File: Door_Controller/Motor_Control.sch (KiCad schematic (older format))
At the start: 15 parts

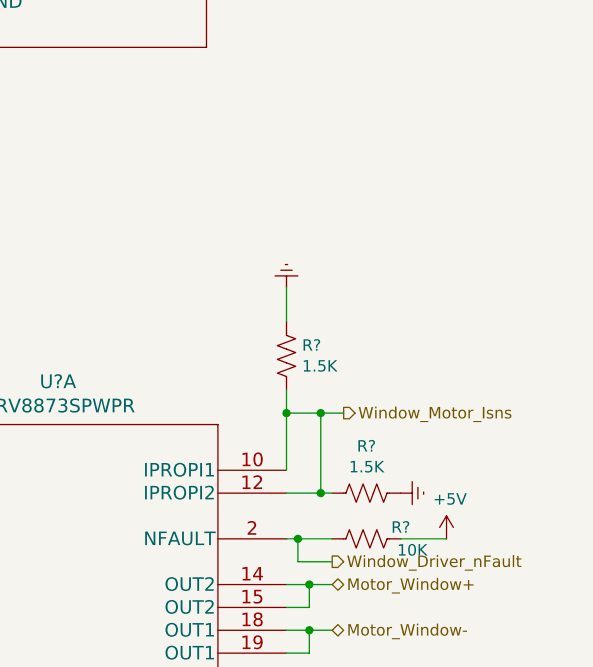
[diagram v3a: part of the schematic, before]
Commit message: differential window motor current sense output in motor control sheet
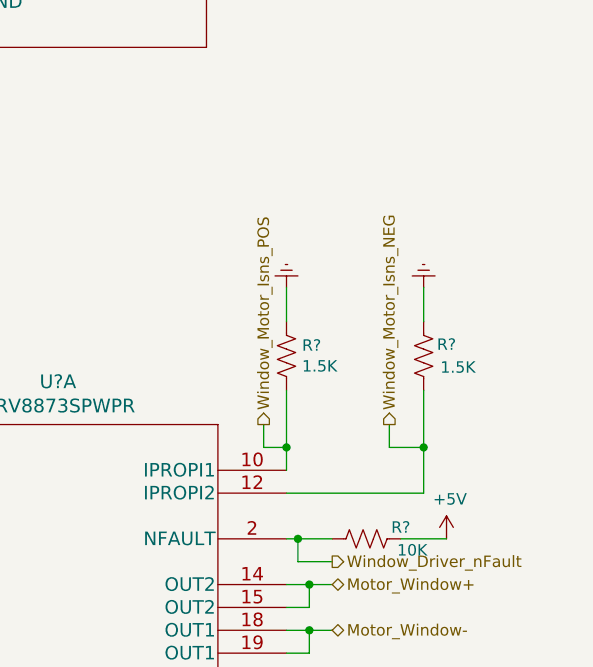
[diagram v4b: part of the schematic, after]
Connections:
- net Window_Motor_Isns renamed Window_Motor_Isns_NEG
- net Window_Motor_Isns_NEG: no longer R?.2, U?.10 (IPROPI1)
- new net Window_Motor_Isns_POS: R?.2, U?.10 (IPROPI1)
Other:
- moved on the sheet: R?
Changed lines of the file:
@@
 L power:Earth #PWR?
 U 1 1 5FB97E86
-P 5300 4650
-F 0 "#PWR?" H 5300 4400 50  0001 C CNN
-F 1 "Earth" H 5300 4500 50  0001 C CNN
-F 2 "" H 5300 4650 50  0001 C CNN
-F 3 "~" H 5300 4650 50  0001 C CNN
-	1    5300 4650
-	0    -1   -1   0
+P 5400 3750
+F 0 "#PWR?" H 5400 3500 50  0001 C CNN
+F 1 "Earth" H 5400 3600 50  0001 C CNN
+F 2 "" H 5400 3750 50  0001 C CNN
+F 3 "~" H 5400 3750 50  0001 C CNN
+	1    5400 3750
+	-1   0    0    1
 $EndComp
 $Comp
@@
 Wire Notes Line
 	3050 5900 3050 5500
-Text HLabel 5050 4300 2    50   Output ~ 0
-Window_Motor_Isns
 Wire Wire Line
 	2650 5550 2800 5550
@@
 Wire Wire Line
 	5000 5550 4800 5550
-$Comp
-L Device:R_US R?
-U 1 1 5FB94200
-P 4800 4050
-F 0 "R?" H 4868 4096 50  0000 L CNN
-F 1 "1.5K" H 4868 4005 50  0000 L CNN
-F 2 "" V 4840 4040 50  0001 C CNN
-F 3 "~" H 4800 4050 50  0001 C CNN
-	1    4800 4050
-	1    0    0    -1
-$EndComp
-$Comp
-L power:Earth #PWR?
-U 1 1 5FB972EF
-P 4800 3750
-F 0 "#PWR?" H 4800 3500 50  0001 C CNN
-F 1 "Earth" H 4800 3600 50  0001 C CNN
-F 2 "" H 4800 3750 50  0001 C CNN
-F 3 "~" H 4800 3750 50  0001 C CNN
-	1    4800 3750
-	-1   0    0    1
-$EndComp
-Wire Wire Line
-	4800 4650 4950 4650
-Wire Wire Line
-	4800 3900 4800 3750
-Connection ~ 4800 4300
-Wire Wire Line
-	4800 4300 4800 4200
-Wire Wire Line
-	4950 4650 4950 4300
-Connection ~ 4950 4650
-Wire Wire Line
-	4950 4650 5000 4650
-Connection ~ 4950 4300
-Wire Wire Line
-	4950 4300 4800 4300
-Wire Wire Line
-	5050 4300 4950 4300
 Text HLabel 5000 4950 2    50   Output ~ 0
 Window_Driver_nFault
@@
 Wire Wire Line
 	4850 4850 5000 4850
-Wire Wire Line
-	4800 4550 4800 4300
+$Comp
+L Device:R_US R?
+U 1 1 5FB96318
+P 5400 4050
+F 0 "R?" H 5500 4100 50  0000 C CNN
+F 1 "1.5K" H 5550 4000 50  0000 C CNN
+F 2 "" V 5440 4040 50  0001 C CNN
+F 3 "~" H 5400 4050 50  0001 C CNN
+	1    5400 4050
+	1    0    0    -1
+$EndComp
+$Comp
+L power:Earth #PWR?
+U 1 1 5FBE9744
+P 2300 4650
+F 0 "#PWR?" H 2300 4400 50  0001 C CNN
+F 1 "Earth" H 2300 4500 50  0001 C CNN
+F 2 "" H 2300 4650 50  0001 C CNN
+F 3 "~" H 2300 4650 50  0001 C CNN
+	1    2300 4650
+	0    1    1    0
+$EndComp
+$Comp
+L power:Earth #PWR?
+U 1 1 5FBEA1C6
+P 2300 4950
+F 0 "#PWR?" H 2300 4700 50  0001 C CNN
+F 1 "Earth" H 2300 4800 50  0001 C CNN
+F 2 "" H 2300 4950 50  0001 C CNN
+F 3 "~" H 2300 4950 50  0001 C CNN
+	1    2300 4950
+	0    1    1    0
+$EndComp
+$Comp
+L Device:R_US R?
+U 1 1 5FBEA830
+P 2550 4950
+F 0 "R?" V 2600 5100 50  0000 C CNN
+F 1 "1.5K" V 2500 5100 50  0000 C CNN
+F 2 "" V 2590 4940 50  0001 C CNN
+F 3 "~" H 2550 4950 50  0001 C CNN
+	1    2550 4950
+	0    1    1    0
+$EndComp
+Wire Wire Line
+	2700 4950 2800 4950
+Wire Wire Line
+	2400 4950 2300 4950
+$Comp
+L Device:R_US R?
+U 1 1 5FBED892
+P 2550 4650
+F 0 "R?" V 2600 4800 50  0000 C CNN
+F 1 "1.5K" V 2500 4800 50  0000 C CNN
+F 2 "" V 2590 4640 50  0001 C CNN
+F 3 "~" H 2550 4650 50  0001 C CNN
+	1    2550 4650
+	0    1    1    0
+$EndComp
+Wire Wire Line
+	2300 4650 2400 4650
+Wire Wire Line
+	2700 4650 2800 4650
+$Comp
+L power:Earth #PWR?
+U 1 1 5FBF1639
+P 1400 5400
+F 0 "#PWR?" H 1400 5150 50  0001 C CNN
+F 1 "Earth" H 1400 5250 50  0001 C CNN
+F 2 "" H 1400 5400 50  0001 C CNN
+F 3 "~" H 1400 5400 50  0001 C CNN
+	1    1400 5400
+	1    0    0    -1
+$EndComp
+$Comp
+L Device:C C?
+U 1 1 5FBF1C79
+P 1400 5150
+F 0 "C?" H 1515 5196 50  0000 L CNN
+F 1 "1uF" H 1515 5105 50  0000 L CNN
+F 2 "" H 1438 5000 50  0001 C CNN
+F 3 "~" H 1400 5150 50  0001 C CNN
+	1    1400 5150
+	1    0    0    -1
+$EndComp
+$Comp
+L power:+5V #PWR?
+U 1 1 5FBF2E2E
+P 1400 4800
+F 0 "#PWR?" H 1400 4650 50  0001 C CNN
+F 1 "+5V" H 1415 4973 50  0000 C CNN
+F 2 "" H 1400 4800 50  0001 C CNN
+F 3 "" H 1400 4800 50  0001 C CNN
+	1    1400 4800
+	1    0    0    -1
+$EndComp
+Wire Wire Line
+	1400 5400 1400 5300
+Wire Wire Line
+	1400 5000 1400 4850
+Wire Wire Line
+	2800 4850 1400 4850
+Connection ~ 1400 4850
+Wire Wire Line
+	1400 4850 1400 4800
+Text HLabel 2350 4550 0    50   Input ~ 0
+Window_Ctrl_nDisable
+$Comp
+L Device:C C?
+U 1 1 5FBF9A3D
+P 2500 4300
+F 0 "C?" H 2615 4346 50  0000 L CNN
+F 1 "1uF" H 2615 4255 50  0000 L CNN
+F 2 "" H 2538 4150 50  0001 C CNN
+F 3 "~" H 2500 4300 50  0001 C CNN
+	1    2500 4300
+	1    0    0    -1
+$EndComp
+$Comp
+L power:Earth #PWR?
+U 1 1 5FBFA2FE
+P 2500 4050
+F 0 "#PWR?" H 2500 3800 50  0001 C CNN
+F 1 "Earth" H 2500 3900 50  0001 C CNN
+F 2 "" H 2500 4050 50  0001 C CNN
+F 3 "~" H 2500 4050 50  0001 C CNN
+	1    2500 4050
+	-1   0    0    1
+$EndComp
+Wire Wire Line
+	2500 4050 2500 4150
+Wire Wire Line
+	2350 4550 2500 4550
+Wire Wire Line
+	2500 4450 2500 4550
+Connection ~ 2500 4550
+Wire Wire Line
+	2500 4550 2800 4550
+Wire Wire Line
+	4800 4650 5400 4650
+Wire Wire Line
+	5400 4650 5400 4450
+Wire Wire Line
+	5400 3900 5400 3750
+Text HLabel 4700 4350 1    50   Output ~ 0
+Window_Motor_Isns_POS
+Text HLabel 5250 4350 1    50   Output ~ 0
+Window_Motor_Isns_NEG
+Wire Wire Line
+	4800 4200 4800 4450
 $Comp
 L DRV8873SPWPR:DRV8873SPWPR U?
@@
 	1    0    0    -1
 $EndComp
-$Comp
-L Device:R_US R?
-U 1 1 5FB96318
-P 5150 4650
-F 0 "R?" V 4945 4650 50  0000 C CNN
-F 1 "1.5K" V 5036 4650 50  0000 C CNN
-F 2 "" V 5190 4640 50  0001 C CNN
-F 3 "~" H 5150 4650 50  0001 C CNN
-	1    5150 4650
-	0    1    1    0
-$EndComp
-$Comp
-L power:Earth #PWR?
-U 1 1 5FBE9744
-P 2300 4650
-F 0 "#PWR?" H 2300 4400 50  0001 C CNN
-F 1 "Earth" H 2300 4500 50  0001 C CNN
-F 2 "" H 2300 4650 50  0001 C CNN
-F 3 "~" H 2300 4650 50  0001 C CNN
-	1    2300 4650
-	0    1    1    0
-$EndComp
-$Comp
-L power:Earth #PWR?
-U 1 1 5FBEA1C6
-P 2300 4950
-F 0 "#PWR?" H 2300 4700 50  0001 C CNN
-F 1 "Earth" H 2300 4800 50  0001 C CNN
-F 2 "" H 2300 4950 50  0001 C CNN
-F 3 "~" H 2300 4950 50  0001 C CNN
-	1    2300 4950
-	0    1    1    0
-$EndComp
-$Comp
-L Device:R_US R?
-U 1 1 5FBEA830
-P 2550 4950
-F 0 "R?" V 2600 5100 50  0000 C CNN
-F 1 "1.5K" V 2500 5100 50  0000 C CNN
-F 2 "" V 2590 4940 50  0001 C CNN
-F 3 "~" H 2550 4950 50  0001 C CNN
-	1    2550 4950
-	0    1    1    0
-$EndComp
-Wire Wire Line
-	2700 4950 2800 4950
-Wire Wire Line
-	2400 4950 2300 4950
-$Comp
-L Device:R_US R?
-U 1 1 5FBED892
-P 2550 4650
-F 0 "R?" V 2600 4800 50  0000 C CNN
-F 1 "1.5K" V 2500 4800 50  0000 C CNN
-F 2 "" V 2590 4640 50  0001 C CNN
-F 3 "~" H 2550 4650 50  0001 C CNN
-	1    2550 4650
-	0    1    1    0
-$EndComp
-Wire Wire Line
-	2300 4650 2400 4650
-Wire Wire Line
-	2700 4650 2800 4650
-$Comp
-L power:Earth #PWR?
-U 1 1 5FBF1639
-P 1400 5400
-F 0 "#PWR?" H 1400 5150 50  0001 C CNN
-F 1 "Earth" H 1400 5250 50  0001 C CNN
-F 2 "" H 1400 5400 50  0001 C CNN
-F 3 "~" H 1400 5400 50  0001 C CNN
-	1    1400 5400
-	1    0    0    -1
-$EndComp
-$Comp
-L Device:C C?
-U 1 1 5FBF1C79
-P 1400 5150
-F 0 "C?" H 1515 5196 50  0000 L CNN
-F 1 "1uF" H 1515 5105 50  0000 L CNN
-F 2 "" H 1438 5000 50  0001 C CNN
-F 3 "~" H 1400 5150 50  0001 C CNN
-	1    1400 5150
-	1    0    0    -1
-$EndComp
-$Comp
-L power:+5V #PWR?
-U 1 1 5FBF2E2E
-P 1400 4800
-F 0 "#PWR?" H 1400 4650 50  0001 C CNN
-F 1 "+5V" H 1415 4973 50  0000 C CNN
-F 2 "" H 1400 4800 50  0001 C CNN
-F 3 "" H 1400 4800 50  0001 C CNN
-	1    1400 4800
-	1    0    0    -1
-$EndComp
-Wire Wire Line
-	1400 5400 1400 5300
-Wire Wire Line
-	1400 5000 1400 4850
-Wire Wire Line
-	2800 4850 1400 4850
-Connection ~ 1400 4850
-Wire Wire Line
-	1400 4850 1400 4800
-Text HLabel 2350 4550 0    50   Input ~ 0
-Window_Ctrl_nDisable
-$Comp
-L Device:C C?
-U 1 1 5FBF9A3D
-P 2500 4300
-F 0 "C?" H 2615 4346 50  0000 L CNN
-F 1 "1uF" H 2615 4255 50  0000 L CNN
-F 2 "" H 2538 4150 50  0001 C CNN
-F 3 "~" H 2500 4300 50  0001 C CNN
-	1    2500 4300
-	1    0    0    -1
-$EndComp
-$Comp
-L power:Earth #PWR?
-U 1 1 5FBFA2FE
-P 2500 4050
-F 0 "#PWR?" H 2500 3800 50  0001 C CNN
-F 1 "Earth" H 2500 3900 50  0001 C CNN
-F 2 "" H 2500 4050 50  0001 C CNN
-F 3 "~" H 2500 4050 50  0001 C CNN
-	1    2500 4050
-	-1   0    0    1
-$EndComp
-Wire Wire Line
-	2500 4050 2500 4150
-Wire Wire Line
-	2350 4550 2500 4550
-Wire Wire Line
-	2500 4450 2500 4550
-Connection ~ 2500 4550
-Wire Wire Line
-	2500 4550 2800 4550
+Wire Wire Line
+	4800 3900 4800 3750
+$Comp
+L power:Earth #PWR?
+U 1 1 5FB972EF
+P 4800 3750
+F 0 "#PWR?" H 4800 3500 50  0001 C CNN
+F 1 "Earth" H 4800 3600 50  0001 C CNN
+F 2 "" H 4800 3750 50  0001 C CNN
+F 3 "~" H 4800 3750 50  0001 C CNN
+	1    4800 3750
+	-1   0    0    1
+$EndComp
+$Comp
+L Device:R_US R?
+U 1 1 5FB94200
+P 4800 4050
+F 0 "R?" H 4868 4096 50  0000 L CNN
+F 1 "1.5K" H 4868 4005 50  0000 L CNN
+F 2 "" V 4840 4040 50  0001 C CNN
+F 3 "~" H 4800 4050 50  0001 C CNN
+	1    4800 4050
+	1    0    0    -1
+$EndComp
+Wire Wire Line
+	4800 4450 4700 4450
+Wire Wire Line
+	4700 4450 4700 4350
+Connection ~ 4800 4450
+Wire Wire Line
+	4800 4450 4800 4550
+Wire Wire Line
+	5250 4350 5250 4450
+Wire Wire Line
+	5250 4450 5400 4450
+Connection ~ 5400 4450
+Wire Wire Line
+	5400 4450 5400 4200
 $EndSCHEMATC

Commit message: reorg motor_control
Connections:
- net Window_Motor_Isns_NEG renamed Window_Motor_Imon_NEG
- net Window_Motor_Isns_POS renamed Window_Motor_Imon_POS
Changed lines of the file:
@@
 Text HLabel 2350 4750 0    50   Input ~ 0
 SPI_nCS_Window
-Text HLabel 5000 5050 2    50   BiDi ~ 0
+Text HLabel 5300 5050 2    50   BiDi ~ 0
 Motor_Window+
-Text HLabel 5000 5250 2    50   BiDi ~ 0
-Motor_Window-
-Wire Wire Line
-	5000 5050 4900 5050
-Wire Wire Line
-	5000 5250 4900 5250
 Wire Wire Line
 	4900 5350 4900 5250
-Connection ~ 4900 5250
 Wire Wire Line
 	4900 5150 4900 5050
-Connection ~ 4900 5050
 $Comp
 L power:Earth #PWR?
@@
 	5400 3900 5400 3750
 Text HLabel 4700 4350 1    50   Output ~ 0
-Window_Motor_Isns_POS
+Window_Motor_Imon_POS
 Text HLabel 5250 4350 1    50   Output ~ 0
-Window_Motor_Isns_NEG
+Window_Motor_Imon_NEG
 Wire Wire Line
 	4800 4200 4800 4450
@@
 Wire Wire Line
 	5400 4450 5400 4200
+Text HLabel 5300 5350 2    50   BiDi ~ 0
+Motor_Window-
+Wire Wire Line
+	5300 5350 4900 5350
+Connection ~ 4900 5350
+Wire Wire Line
+	5300 5050 4900 5050
+Connection ~ 4900 5050
 $EndSCHEMATC

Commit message: annotate large traces on window motor driver
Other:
- note added: "Large Traces"
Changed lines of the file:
@@
 Text Notes 2300 2950 1    50   ~ 0
 Ceramic Cap
-Text HLabel 1400 2300 0    50   Input ~ 0
-Fused_12V_Window
 Connection ~ 2400 2400
 Connection ~ 1950 2300
-Text Notes 800  2500 0    50   ~ 0
-Large Trace
 Wire Wire Line
 	1750 2300 1550 2300
@@
 Wire Notes Line
 	1800 2500 1800 2200
-Wire Notes Line
-	1800 2200 800  2200
-Wire Notes Line
-	800  2200 800  2500
-Wire Notes Line
-	800  2500 1800 2500
 Text HLabel 2350 5150 0    50   Input ~ 0
 SPI_MOSI
@@
 	5300 5050 4900 5050
 Connection ~ 4900 5050
+Wire Notes Line
+	1800 2200 800  2200
+Text HLabel 1400 2300 0    50   Input ~ 0
+Fused_12V_Window
+Wire Notes Line
+	4550 5400 4550 5000
+Wire Notes Line
+	4550 5000 6000 5000
+Wire Notes Line
+	6000 5000 6000 5400
+Wire Notes Line
+	6000 5400 4550 5400
+Text Notes 800  2500 0    50   ~ 0
+Large Trace
+Wire Notes Line
+	800  2200 800  2500
+Wire Notes Line
+	800  2500 1800 2500
+Text Notes 5500 5250 0    50   ~ 0
+Large Traces
 $EndSCHEMATC
